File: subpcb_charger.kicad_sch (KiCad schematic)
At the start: 30 parts, among them J10 Screw_Terminal_01x02, J17 Conn_01x02, J19 Conn_01x02, J27 Conn_01x05, J3 Screw_Terminal_01x03, J56 Screw_Terminal_01x02, J57 Conn_01x02, J58 Screw_Terminal_01x02, J59 Conn_01x02, J60 Screw_Terminal_01x02, J61 Conn_01x02, J62 Screw_Terminal_01x02, J63 Conn_01x02, J9 Conn_01x02, U14 Fuse Holder, U15 Fuse Holder, U16 Fuse Holder, U17 Fuse Holder, U72 Jumper Red, U73 Jumper Blue, U74 Fuse 2A, U75 Fuse 2A

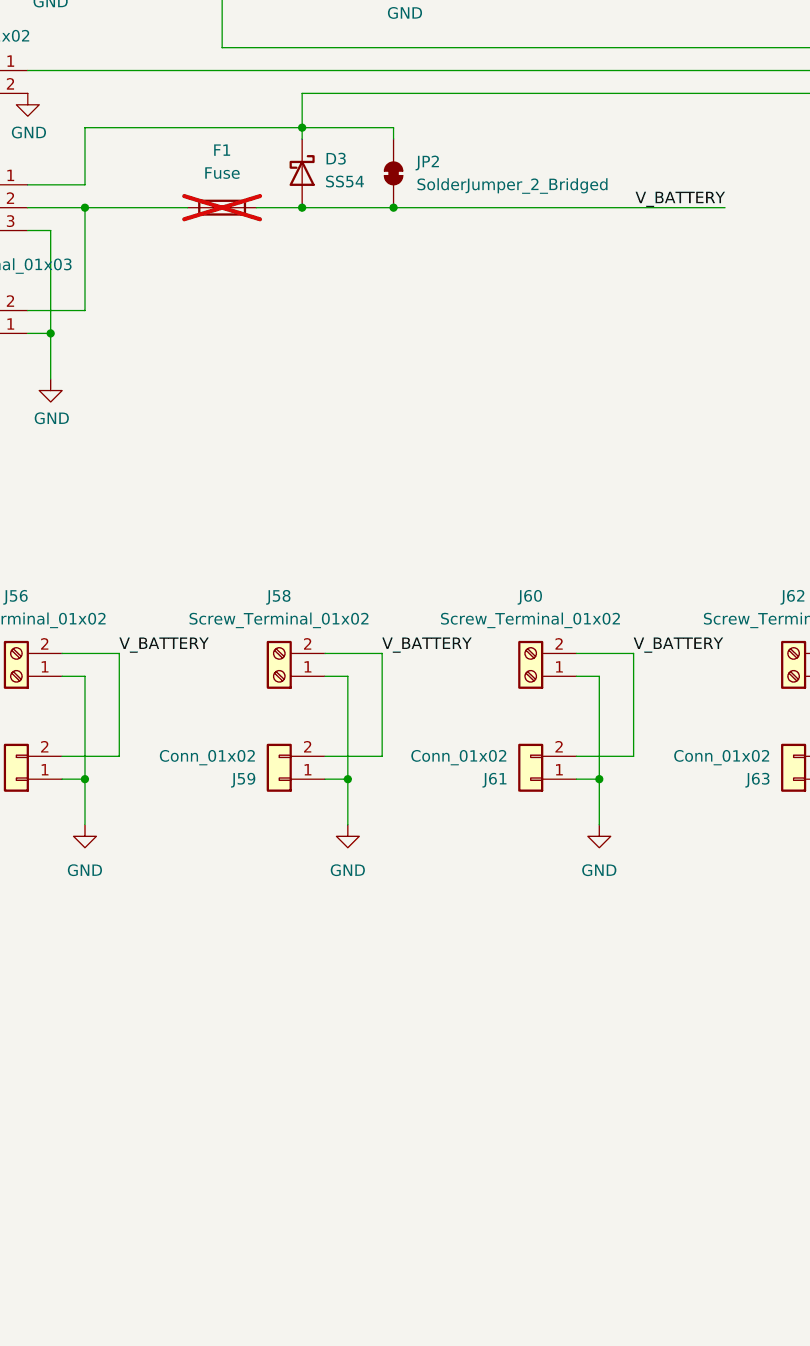
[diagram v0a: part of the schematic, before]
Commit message: New conns for xESC
Added new connectors into the design for motors.
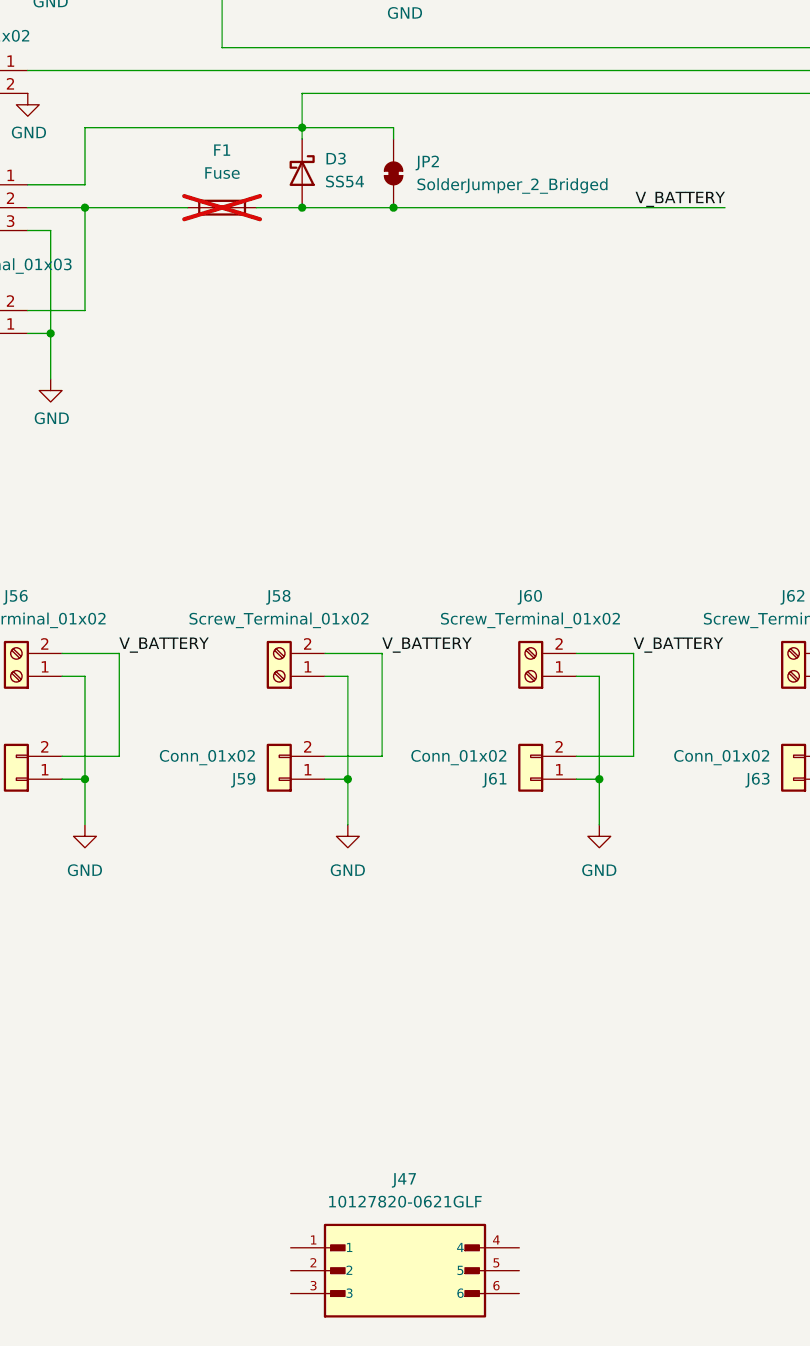
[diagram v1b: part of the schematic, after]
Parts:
- added J47: 10127820-0621GLF, 10127820_0621GLF:AMPHENOL_10127820-0621GLF, symbol 10127820-0621GLF:10127820-0621GLF
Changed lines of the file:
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@@
 (kicad_sch
-	(version 20231120)
+	(version 20250114)
 	(generator "eeschema")
-	(generator_version "8.0")
+	(generator_version "9.0")
 	(paper "A3")
+	(rectangle
+		(start 182.88 -3.81)
+		(end 359.41 50.8)
+		(stroke
+			(width 0)
+			(type default)
+		)
+		(fill
+			(type none)
+		)
+	)
+	(text "Connectors to join the PCBs when separated.\nAll hierachical inputs need to be here in order to restore the connections."
+		(exclude_from_sim no)
+		(at 198.628 -13.462 0)
+		(effects
+			(font
+				(size 1.27 1.27)
+			)
+		)
+	)
 	(junction
 		(at 92.71 83.82)
@@
 		)
 	)
-	(rectangle
-		(start 182.88 -3.81)
-		(end 359.41 50.8)
-		(stroke
-			(width 0)
-			(type default)
-		)
-		(fill
-			(type none)
-		)
-	)
-	(text "Connectors to join the PCBs when separated.\nAll hierachical inputs need to be here in order to restore the connections."
-		(exclude_from_sim no)
-		(at 198.628 -13.462 0)
-		(effects
-			(font
-				(size 1.27 1.27)
-			)
-		)
-	)
 	(label "5V"
 		(at 167.64 72.39 0)
-		(fields_autoplaced yes)
 		(effects
 			(font
@@
 	(label "5V"
 		(at 58.42 31.75 180)
-		(fields_autoplaced yes)
 		(effects
 			(font
@@
 	(label "V_BATTERY"
 		(at 72.39 142.24 0)
-		(fields_autoplaced yes)
 		(effects
 			(font
@@
 	(label "V_BATTERY"
 		(at 139.7 92.71 180)
-		(fields_autoplaced yes)
 		(effects
 			(font
@@
 	(label "V_BATTERY"
 		(at 158.75 142.24 0)
-		(fields_autoplaced yes)
 		(effects
 			(font
@@
 	(label "I2C{SDA SCL}"
 		(at 58.42 27.94 180)
-		(fields_autoplaced yes)
 		(effects
 			(font
@@
 	(label "I2C{SDA SCL}"
 		(at 229.87 82.55 0)
-		(fields_autoplaced yes)
 		(effects
 			(font
@@
 	(label "V_BATTERY"
 		(at 129.54 142.24 0)
-		(fields_autoplaced yes)
 		(effects
 			(font
@@
 	(label "V_CHARGE"
 		(at 167.64 74.93 0)
-		(fields_autoplaced yes)
 		(effects
 			(font
@@
 	(label "V_BATTERY"
 		(at 58.42 20.32 180)
-		(fields_autoplaced yes)
 		(effects
 			(font
@@
 	(label "5V"
 		(at 191.77 13.97 0)
-		(fields_autoplaced yes)
 		(effects
 			(font
@@
 	(label "V_BATTERY"
 		(at 101.6 142.24 0)
-		(fields_autoplaced yes)
 		(effects
 			(font
@@
 	(label "V_CHARGE_SENSE"
 		(at 104.14 39.37 0)
-		(fields_autoplaced yes)
 		(effects
 			(font
@@
 	(label "I2C.SCL"
 		(at 191.77 19.05 0)
-		(fields_autoplaced yes)
 		(effects
 			(font
@@
 	(label "I2C.SDA"
 		(at 191.77 16.51 0)
-		(fields_autoplaced yes)
 		(effects
 			(font
@@
 	(label "V_CHARGE_SENSE"
 		(at 58.42 24.13 180)
-		(fields_autoplaced yes)
 		(effects
 			(font
@@
 	(label "V_CHARGE_SENSE"
 		(at 191.77 21.59 0)
-		(fields_autoplaced yes)
 		(effects
 			(font
@@
 		(shape input)
 		(at 38.1 24.13 180)
-		(fields_autoplaced yes)
 		(effects
 			(font
@@
 		(shape input)
 		(at 38.1 27.94 180)
-		(fields_autoplaced yes)
 		(effects
 			(font
@@
 		(shape input)
 		(at 38.1 31.75 180)
-		(fields_autoplaced yes)
 		(effects
 			(font
@@
 		(shape output)
 		(at 38.1 20.32 180)
-		(fields_autoplaced yes)
 		(effects
 			(font
@@
 	)
 	(symbol
+		(lib_id "10127820-0621GLF:10127820-0621GLF")
+		(at 104.14 210.82 0)
+		(unit 1)
+		(exclude_from_sim no)
+		(in_bom yes)
+		(on_board yes)
+		(dnp no)
+		(fields_autoplaced yes)
+		(property "Reference" "J47"
+			(at 104.14 200.66 0)
+			(effects
+				(font
+					(size 1.27 1.27)
+				)
+			)
+		)
+		(property "Value" "10127820-0621GLF"
+			(at 104.14 203.2 0)
+			(effects
+				(font
+					(size 1.27 1.27)
+				)
+			)
+		)
+		(property "Footprint" "10127820_0621GLF:AMPHENOL_10127820-0621GLF"
+			(at 104.14 210.82 0)
+			(effects
+				(font
+					(size 1.27 1.27)
+				)
+				(justify bottom)
+				(hide yes)
+			)
+		)
+		(property "Datasheet" ""
+			(at 104.14 210.82 0)
+			(effects
+				(font
+					(size 1.27 1.27)
+				)
+				(hide yes)
+			)
+		)
+		(property "Description" ""
+			(at 104.14 210.82 0)
+			(effects
+				(font
+					(size 1.27 1.27)
+				)
+				(hide yes)
+			)
+		)
+		(property "PARTREV" "R"
+			(at 104.14 210.82 0)
+			(effects
+				(font
+					(size 1.27 1.27)
+				)
+				(justify bottom)
+				(hide yes)
+			)
+		)
+		(property "MANUFACTURER" "Amphenol"
+			(at 104.14 210.82 0)
+			(effects
+				(font
+					(size 1.27 1.27)
+				)
+				(justify bottom)
+				(hide yes)
+			)
+		)
+		(property "MAXIMUM_PACKAGE_HEIGHT" "12.80 mm"
+			(at 104.14 210.82 0)
+			(effects
+				(font
+					(size 1.27 1.27)
+				)
+				(justify bottom)
+				(hide yes)
+			)
+		)
+		(property "STANDARD" "Manufacturer Recommendations"
+			(at 104.14 210.82 0)
+			(effects
+				(font
+					(size 1.27 1.27)
+				)
+				(justify bottom)
+				(hide yes)
+			)
+		)
+		(property "Digikey PN" "609-10127820-0621GLF-ND"
+			(at 104.14 210.82 0)
+			(effects
+				(font
+					(size 1.27 1.27)
+				)
+				(hide yes)
+			)
+		)
+		(pin "2"
+		)
+		(pin "3"
+		)
+		(pin "5"
+		)
+		(pin "1"
+		)
+		(pin "6"
+		)
+		(pin "4"
+		)
+		(instances
+			(project ""
+				(path "/e12e8a63-1d1b-4736-9aba-a87a258b2b11/2930b75f-7142-4414-b99a-728851a6a7da"
+					(reference "J47")
+					(unit 1)
+				)
+			)
+		)
+	)
+	(symbol
 		(lib_id "Connector_Generic:Conn_01x05")
 		(at 217.17 19.05 0)
@@
 		(at 182.88 66.04)
 		(size 36.83 20.32)
+		(exclude_from_sim no)
+		(in_bom yes)
+		(on_board yes)
+		(dnp no)
 		(fields_autoplaced yes)
 		(stroke

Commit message: Routing progress
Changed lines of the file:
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@@
-	(wire
-		(pts
-			(xy 38.1 24.13) (xy 58.42 24.13)
-		)
-		(stroke
-			(width 0)
-			(type default)
-		)
-	)
 	(wire
 		(pts
@@
 	(wire
 		(pts
-			(xy 58.42 20.32) (xy 38.1 20.32)
-		)
-		(stroke
-			(width 0)
-			(type default)
-		)
-	)
-	(wire
-		(pts
 			(xy 191.77 19.05) (xy 212.09 19.05)
 		)
@@
 	(wire
 		(pts
-			(xy 38.1 31.75) (xy 58.42 31.75)
-		)
-		(stroke
-			(width 0)
-			(type default)
-		)
-	)
-	(wire
-		(pts
 			(xy 104.14 64.77) (xy 104.14 63.5)
 		)
@@
 		(pts
 			(xy 66.04 142.24) (xy 72.39 142.24)
-		)
-		(stroke
-			(width 0)
-			(type default)
-		)
-	)
-	(bus
-		(pts
-			(xy 38.1 27.94) (xy 58.42 27.94)
 		)
 		(stroke
@@
 		)
 	)
-	(label "5V"
-		(at 58.42 31.75 180)
-		(effects
-			(font
-				(size 1.27 1.27)
-			)
-			(justify right bottom)
-		)
-	)
 	(label "V_BATTERY"
 		(at 72.39 142.24 0)
@@
 	)
 	(label "I2C{SDA SCL}"
-		(at 58.42 27.94 180)
-		(effects
-			(font
-				(size 1.27 1.27)
-			)
-			(justify right bottom)
-		)
-	)
-	(label "I2C{SDA SCL}"
 		(at 229.87 82.55 0)
 		(effects
@@
 		)
 	)
-	(label "V_BATTERY"
-		(at 58.42 20.32 180)
-		(effects
-			(font
-				(size 1.27 1.27)
-			)
-			(justify right bottom)
-		)
-	)
 	(label "5V"
 		(at 191.77 13.97 0)
@@
 	)
 	(label "V_CHARGE_SENSE"
-		(at 58.42 24.13 180)
-		(effects
-			(font
-				(size 1.27 1.27)
-			)
-			(justify right bottom)
-		)
-	)
-	(label "V_CHARGE_SENSE"
 		(at 191.77 21.59 0)
 		(effects
@@
 		)
 	)
-	(hierarchical_label "V_CHARGE_SENSE"
-		(shape input)
-		(at 38.1 24.13 180)
-		(effects
-			(font
-				(size 1.27 1.27)
-			)
-			(justify right)
-		)
-	)
-	(hierarchical_label "I2C{SDA SCL}"
-		(shape input)
-		(at 38.1 27.94 180)
-		(effects
-			(font
-				(size 1.27 1.27)
-			)
-			(justify right)
-		)
-	)
-	(hierarchical_label "5V"
-		(shape input)
-		(at 38.1 31.75 180)
-		(effects
-			(font
-				(size 1.27 1.27)
-			)
-			(justify right)
-		)
-	)
-	(hierarchical_label "V_BATTERY"
-		(shape output)
-		(at 38.1 20.32 180)
-		(effects
-			(font
-				(size 1.27 1.27)
-			)
-			(justify right)
-		)
-	)

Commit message: Routing progress
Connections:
- net Charger/NTC_BATT is gone; now on net NTC_BATT: J19.1 (Pin_1)
- net GND: now also J47.1, J47.2, J47.6
- net V_CHARGE_PFUSE: now reaches F2.1, J10.2 (Pin_2), J17.2 (Pin_2)
- net V_CHARGE_PFUSE: now also J47.4
- net V_BATTERY_PFUSE: now reaches F1.1, J3.2 (Pin_2), J9.2 (Pin_2)
- net V_BATTERY_PFUSE: now also J47.3
- net NTC_BATT: now reaches J47.5
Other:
- moved on the sheet: J47
